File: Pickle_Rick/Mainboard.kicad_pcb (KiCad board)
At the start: 4 copper layers, 152 parts, among them J1 USB_C_Receptacle, J10 Conn_01x02_Male, J11 Conn_01x02_Male, J12 Conn_01x02_Male, J2 8P8C_LED, J3 Micro_SD_Card_Det, J4 Conn_Coaxial, J5 Conn_Coaxial, J6 Screw_Terminal_01x02, J7 Screw_Terminal_01x02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

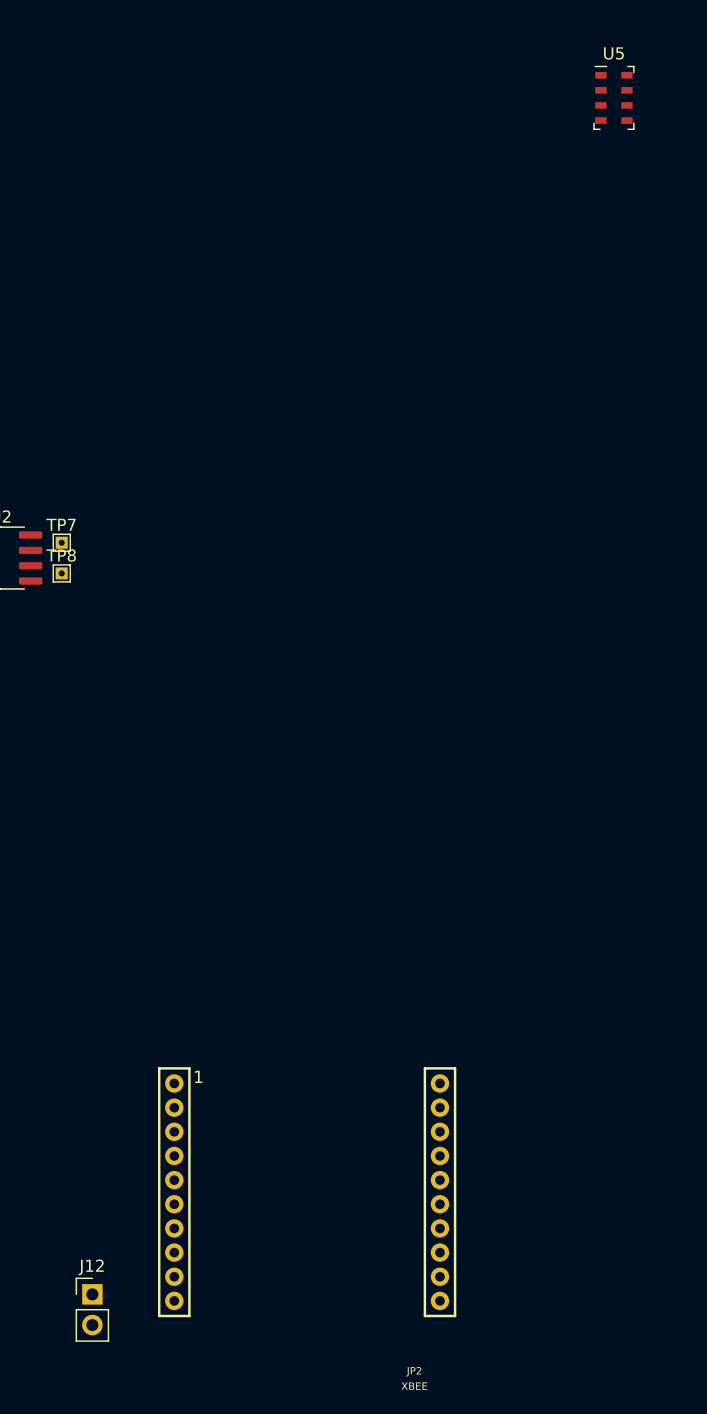
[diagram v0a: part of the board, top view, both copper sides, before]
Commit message: changed usb 2.0 to 3.0; started pcb design; changed flash symbol
need to change flash footprint still
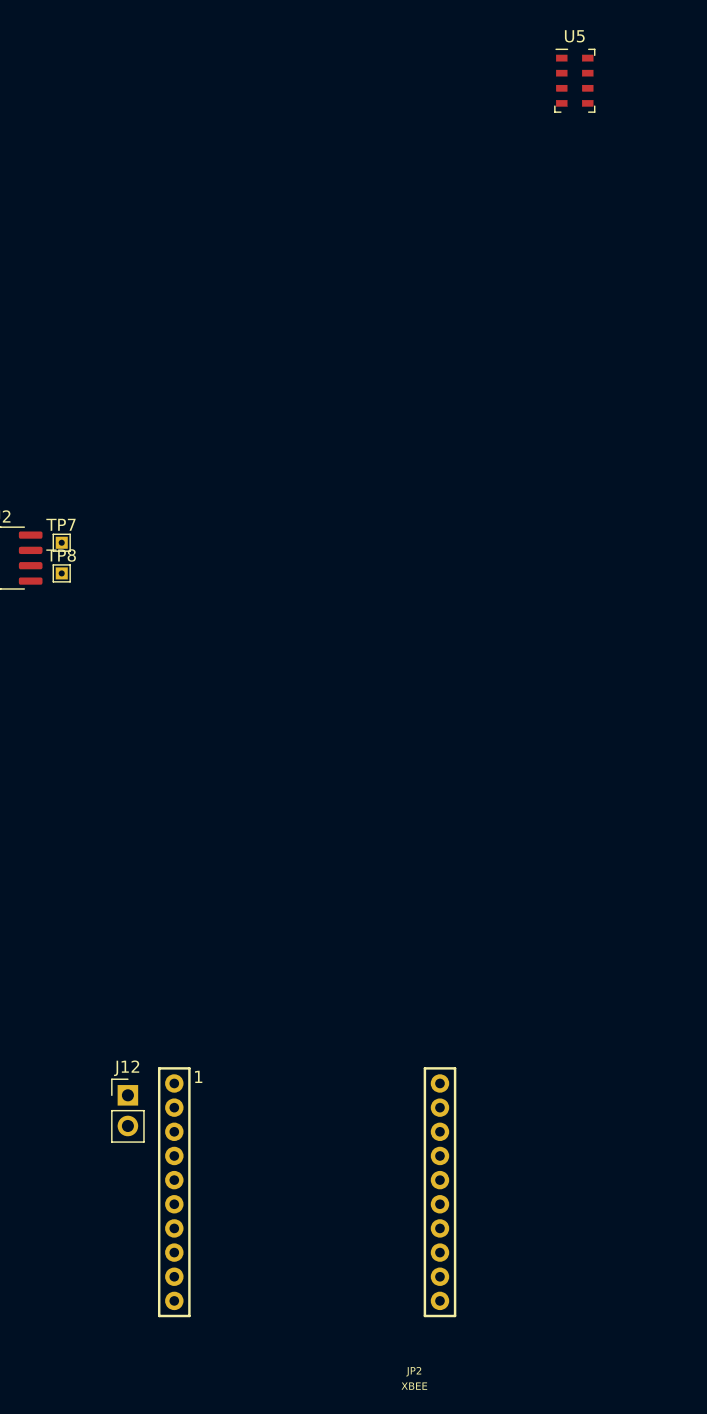
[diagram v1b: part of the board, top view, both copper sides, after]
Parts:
- moved J12 16.7 mm to (229.0, -113.0)
- moved U5 3.54 mm to (266.0, -197.0)
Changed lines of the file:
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@@
   )
   (module Package_LGA:LGA-8_3x5mm_P1.25mm (layer F.Cu)
-    (at 269.24 -195.58)
+    (at 266 -197)
     (descr LGA-8)
     (tags "lga land grid array")
@@
   )
   (module Connector_PinHeader_2.54mm:PinHeader_1x02_P2.54mm_Vertical (layer F.Cu)
-    (at 226.06 -96.52)
+    (at 229 -113)
     (descr "Through hole straight pin header, 1x02, 2.54mm pitch, single row")
     (tags "Through hole pin header THT 1x02 2.54mm single row")

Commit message: did some pcb thing
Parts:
- removed H3, H4: MountingHole_Pad, MountingHole:MountingHole_3.2mm_M3_DIN965_Pad
- removed JP2: XBEE, iclr:XBEE
- BZ1: moved to B.Cu
- D13: value USB_LED -> down_led
- D17: value USB_LED -> up_led
- H1, H2: footprint MountingHole:MountingHole_3.2mm_M3_DIN965_Pad -> MountingHole:MountingHole_2.2mm_M2_Pad
- moved R2 406.9 mm to (24.4, 85.8), turned to 270 degrees
- moved R26 403.7 mm to (40.7, 100.0), turned to 180 degrees
- moved TP23 403.2 mm to (34.6, 96.7)
- moved R39 403.0 mm to (37.5, 97.0), turned to 180 degrees
- moved R40 402.4 mm to (37.6, 92.3), turned to 180 degrees
- moved R1 401.9 mm to (28.8, 85.6), turned to 90 degrees
- moved C2 401.5 mm to (37.6, 80.1)
- moved R37 401.1 mm to (38.2, 99.3), turned to 270 degrees
- moved TP19 398.0 mm to (36.4, 98.8)
- moved TP2 396.1 mm to (35.9, 90.4)
- moved TP22 395.9 mm to (43.2, 100.2)
- moved R8 395.3 mm to (61.0, 98.9), turned to 90 degrees
- moved TP20 394.6 mm to (38.0, 90.4)
- moved H1 393.7 mm to (24.9, 106.7)
- moved TP9 388.8 mm to (59.8, 91.5)
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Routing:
- net /MOSI: track 0.00 -> 16.7 mm
- net /RADIO_TX: track 0.00 -> 15.3 mm
- net /MISO: track 0.00 -> 14.8 mm, vias 0 -> 1
- net /LORA_RESET: track 0.00 -> 13.7 mm, vias 0 -> 2
- net /RADIO_RX: track 0.00 -> 10.8 mm
- net /LORA_CS: track 0.00 -> 10.3 mm
- net /Cont2: track 0.00 -> 5.79 mm, vias 0 -> 1
- net /BOOT: track 0.00 -> 5.72 mm, vias 0 -> 1
- net /Cont1: track 0.00 -> 5.64 mm, vias 0 -> 1
- net /SCL: track 0.00 -> 5.41 mm
- net /SDA: track 0.00 -> 4.54 mm
- net /RXD: track 0.00 -> 4.06 mm, vias 0 -> 1
- net /TXD: track 0.00 -> 4.00 mm, vias 0 -> 1
- net +3V3: track 0.00 -> 3.92 mm
- net /SCLK: track 0.00 -> 2.77 mm
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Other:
- board outline added: 100 x 30 mm

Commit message: added critical silkscreen + circuitry around esp mostly done
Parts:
- added G***: LOGO, iclr:pccRicc650dpi, F.Cu at (102.8, 139.4)
- added G***: LOGO, iclr:iclr_logo, F.Cu at (113.0, 134.3)
- moved U10 376.8 mm to (77.2, 31.0)
- moved TP4 358.5 mm to (29.2, 84.3)
- moved TP5 358.5 mm to (25.2, 84.3)
- moved TP6 355.4 mm to (27.3, 86.6)
- moved R4 350.8 mm to (34.0, 88.1)
- moved D1 345.3 mm to (32.7, 82.0), turned to 180 degrees
- moved R3 344.5 mm to (39.0, 86.0)
- moved R6 339.6 mm to (42.1, 86.0), turned to 180 degrees
- moved TP3 338.5 mm to (48.8, 85.5)
- moved D9 325.5 mm to (51.1, 86.3)
- moved R25 322.3 mm to (113.7, 86.5), turned to 180 degrees
- moved C4 320.3 mm to (113.7, 84.9), turned to 180 degrees
- moved J4 319.6 mm to (114.4, 82.0), turned to 90 degrees
- moved L1 315.9 mm to (116.1, 85.7), turned to 270 degrees
- moved U6 308.7 mm to (116.7, 93.4), turned to 90 degrees
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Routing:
- net +3V3: track 3.92 -> 36.0 mm, vias 0 -> 4
- net GND: track 0.00 -> 23.6 mm
- net /EN: track 0.00 -> 12.4 mm
- net /MAG_CS: track 0.00 -> 10.7 mm
- net /LORA_RESET: track 13.7 -> 3.53 mm
- net Net-(C3-Pad1): track 1.44 -> 9.90 mm
- net /MISO: track 14.8 -> 6.63 mm
- net /DTR: track 0.00 -> 6.74 mm
- net /CAN_TX: track 0.00 -> 6.70 mm
- net Net-(R16-Pad2): track 0.00 -> 6.53 mm
- net /IMU_CS: track 0.00 -> 5.26 mm
- net /SD_CS: track 0.00 -> 5.18 mm
- net Net-(D15-Pad1): track 0.00 -> 5.02 mm
- net /FLASH_CS: track 0.00 -> 4.58 mm
- net /BARO_CS: track 0.00 -> 4.36 mm
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- added copper zone on In1.Cu, net +3V3
- added copper zone on B.Cu, net GND
- added copper zone on In2.Cu, net GND
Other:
- board text added: "Apes togheter strong"
- board text added: "Based on:"
- board text added: "Designed by:"
- board text added: "Luis Marques Joao Matias"
- board text added: "MUST PLACE THESE 3 ON TOP"
- board text added: "RiCaRdO"

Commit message: not getting farther...
need to double check the buzzer, DS suggests 2 resistors
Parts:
- removed G***: LOGO, iclr:pccRicc650dpi
- removed G***: LOGO, iclr:iclr_logo
- added R43: 1k, Resistor_SMD:R_0603_1608Metric, F.Cu at (42.3, 118.3)
- moved J1 449.8 mm to (28.2, 84.8), turned to 270 degrees
- moved D13 445.4 mm to (31.3, 91.9)
- moved D17 445.4 mm to (31.3, 93.9)
- moved R42 444.9 mm to (35.9, 94.4), turned to 90 degrees
- moved R41 443.3 mm to (36.9, 85.5)
- moved C5 416.5 mm to (55.9, 102.8), turned to 90 degrees
- moved C6 415.5 mm to (54.4, 102.8), turned to 90 degrees
- moved C8 403.2 mm to (102.0, 175.3), turned to 180 degrees
- moved C7 401.4 mm to (102.0, 181.4), turned to 180 degrees
- moved C9 400.2 mm to (102.0, 176.8), turned to 180 degrees
- moved J11 398.5 mm to (-14.3, 130.9)
- moved U12 398.4 mm to (-10.4, 131.4)
- moved C22 397.1 mm to (19.7, 130.6), turned to 180 degrees
- moved C17 396.7 mm to (22.7, 130.6), turned to 180 degrees
- moved C19 395.5 mm to (19.6, 121.4), turned to 180 degrees
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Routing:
- net GND: track 23.6 -> 59.8 mm
- net +3V3: track 36.0 -> 60.3 mm, vias 4 -> 5
- net Net-(J5-Pad1): track 0.00 -> 17.6 mm, vias 0 -> 2
- net /SDA: track 4.54 -> 16.0 mm, vias 0 -> 2
- net Net-(JP5-Pad2): track 0.00 -> 10.4 mm
- net /SCL: track 5.41 -> 15.8 mm, vias 0 -> 2
- net Net-(R25-Pad2): track 0.00 -> 8.64 mm
- net Net-(J4-Pad1): track 0.00 -> 8.29 mm
- net /GPS/RXD: track 0.00 -> 8.24 mm
- net /RADIO_RX: track 11.0 -> 2.81 mm
- net Net-(C6-Pad1): track 0.00 -> 7.27 mm
- net /FLASH_CS: track 4.58 -> 10.4 mm, vias 0 -> 1
- net /BOOT: track 5.45 -> 11.2 mm, vias 1 -> 2
- net Net-(R23-Pad2): track 0.00 -> 4.85 mm
- net Net-(D15-Pad1): track 5.02 -> 0.17 mm
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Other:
- board text removed: "MUST PLACE THESE 3 ON TOP"

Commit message: it almost fits (☉_☉) ...
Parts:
- added G***: LOGO, iclr:pccRicc650dpi, F.Cu at (33.4, 159.3)
- added G***: LOGO, iclr:iclr_logo, F.Cu at (47.1, 151.0)
- J11, U12: moved to B.Cu
- moved J3 122.0 mm to (150.1, 101.8)
- moved TP16 114.7 mm to (34.4, 98.4), turned to 180 degrees
- moved C31 114.3 mm to (32.6, 99.4)
- moved C7 113.1 mm to (30.2, 94.0), turned to 0 degrees
- moved C10 111.8 mm to (34.8, 100.2), turned to 180 degrees
- moved U8 110.8 mm to (30.7, 102.8), turned to 180 degrees
- moved C11 110.7 mm to (30.2, 95.5), turned to 0 degrees
- moved C30 108.4 mm to (30.2, 97.1), turned to 0 degrees
- moved TP17 106.7 mm to (103.9, 74.3), turned to 180 degrees
- moved C9 106.1 mm to (30.2, 98.6), turned to 0 degrees
- moved L2 105.7 mm to (34.5, 102.9), turned to 270 degrees
- moved C8 103.9 mm to (30.3, 100.1), turned to 0 degrees
- moved R14 85.8 mm to (32.5, 96.4), turned to 270 degrees
- moved D6 85.5 mm to (33.5, 94.0)
- moved D12 65.9 mm to (49.1, 99.5), turned to 90 degrees
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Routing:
- net Net-(C6-Pad1): track 7.27 -> 106.5 mm, vias 0 -> 2
- net /MAG_CS: track 9.08 -> 87.3 mm, vias 0 -> 1
- net Net-(C5-Pad1): track 3.95 -> 77.4 mm, vias 0 -> 2
- net /IMU_CS: track 10.00 -> 82.0 mm, vias 0 -> 1
- net GND: track 59.8 -> 126.3 mm
- net /SCLK: track 7.36 -> 59.8 mm
- net /LORA_INT: track 3.61 -> 45.3 mm
- net /MISO: track 9.96 -> 46.3 mm
- net +3V3: track 60.3 -> 95.5 mm, vias 5 -> 8
- net Net-(C1-Pad1): track 2.29 -> 37.5 mm
- net /BOOT: track 11.2 -> 45.3 mm
- net /TXD: track 4.18 -> 37.8 mm
- net /RXD: track 4.44 -> 34.8 mm
- net /usb-c/usb_VBUS: track 3.90 -> 31.3 mm
- net /LORA_RESET: track 4.75 -> 26.0 mm
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- removed copper zone on B.Cu, net GND
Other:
- board size 100 x 30 mm -> 100.1 x 30.1 mm
- board text added: "to the moon"

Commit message: todo: change everything ᕙ(⇀‸↼‶)ᕗ
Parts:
- removed BZ1: Buzzer, Buzzer_Beeper:Buzzer_TDK_PS1240P02BT_D12.2mm_H6.5mm
- removed G***: LOGO, iclr:pccRicc650dpi
- removed G***: LOGO, iclr:iclr_logo
- added J13: Conn_01x02, Connector_JST:JST_XH_B2B-XH-A_1x02_P2.50mm_Vertical, F.Cu at (91.1, 116.5)
- J5: footprint Connector_Coaxial:SMA_Molex_73251-1153_EdgeMount_Horizontal -> Connector_Coaxial:U.FL_Hirose_U.FL-R-SMT-1_Vertical
- J6, J7, J8: footprint iclr:PHOENIX_1757242 -> TerminalBlock_Phoenix:TerminalBlock_Phoenix_PT-1,5-2-5.0-H_1x02_P5.00mm_Horizontal
- moved J5 16.5 mm to (105.3, 68.5)
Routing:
- net /MOSI: track 18.3 -> 5.23 mm
- net /RADIO_TX: track 14.6 -> 4.10 mm
- net GND: track 126.3 -> 116.6 mm
- net /LORA_CS: track 10.2 -> 6.08 mm
- net Net-(J5-Pad1): track 18.3 -> 15.1 mm, vias 2 -> 1

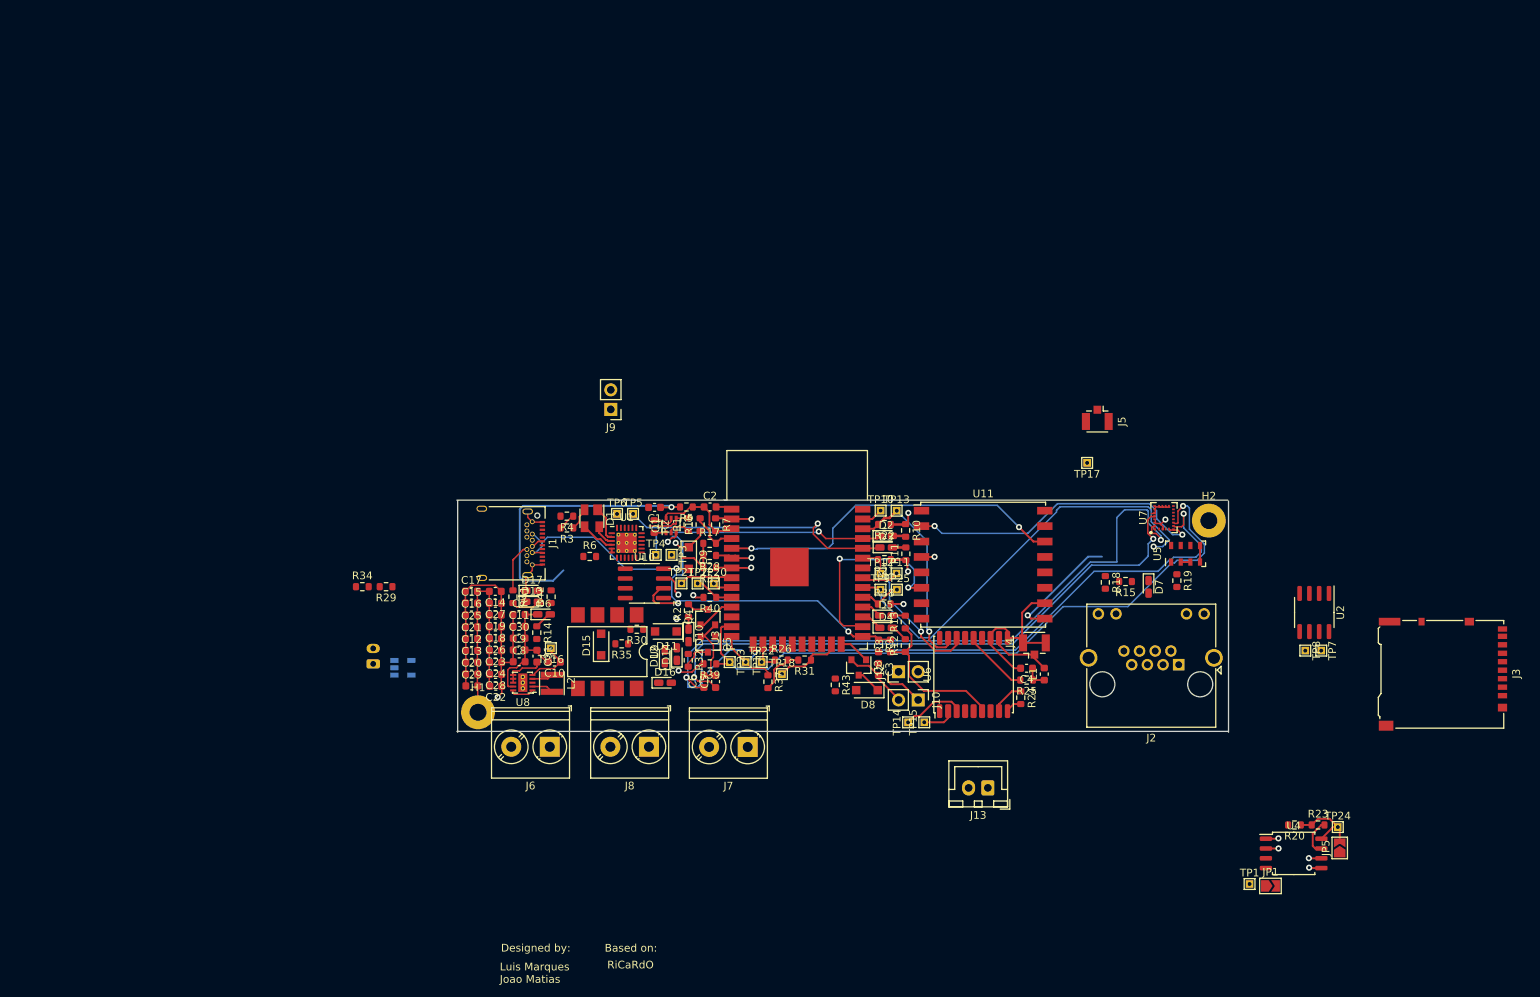
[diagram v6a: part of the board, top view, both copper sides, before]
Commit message: fixed rbg port
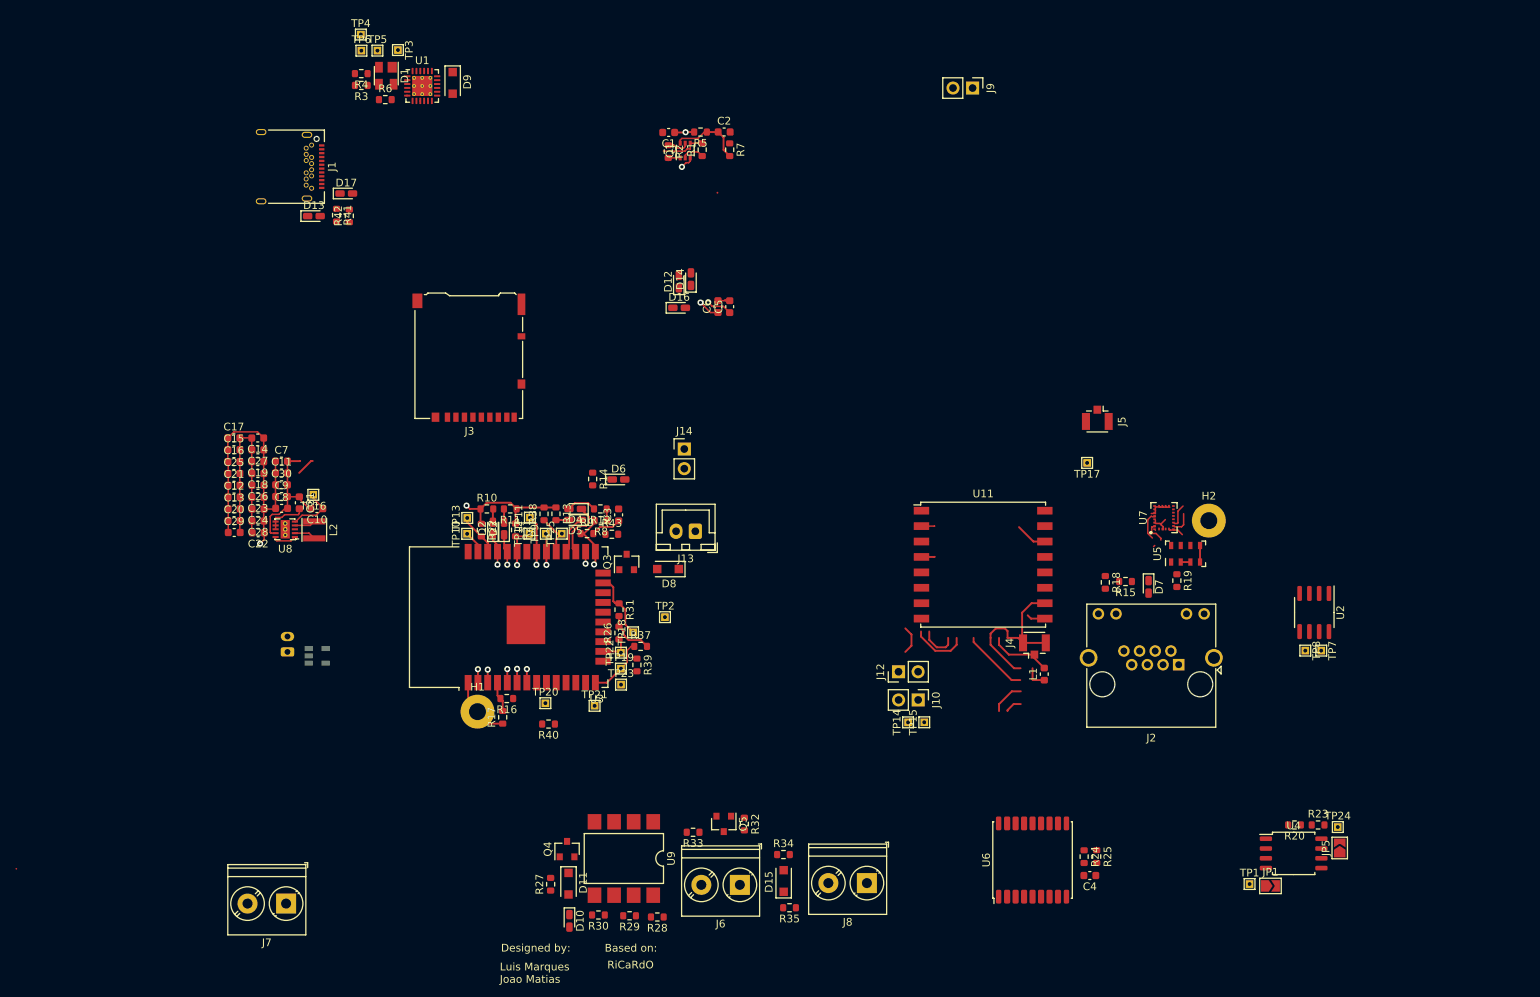
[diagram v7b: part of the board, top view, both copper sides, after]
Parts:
- removed U10: PCA9536D, Package_SO:SOIC-8_3.9x4.9mm_P1.27mm
- added J14: Conn_01x02_Male, Connector_PinHeader_2.54mm:PinHeader_1x02_P2.54mm_Vertical, F.Cu at (51.7, 72.5)
- moved J3 132.9 mm to (23.7, 60.7), turned to 180 degrees
- moved TP4 77.6 mm to (9.72, 18.8)
- moved TP3 74.5 mm to (14.5, 20.8)
- moved D9 68.8 mm to (21.6, 25.0)
- moved TP5 68.6 mm to (11.9, 20.9)
- moved TP6 68.6 mm to (9.79, 20.9)
- moved R6 64.9 mm to (12.9, 27.2)
- moved U1 64.9 mm to (17.7, 25.4)
- moved R34 64.7 mm to (64.5, 125.2)
- moved D1 63.3 mm to (13.0, 24.1)
- moved R3 63.3 mm to (9.78, 25.4)
- moved R4 63.3 mm to (9.78, 23.8)
- moved J7 63.2 mm to (0.02, 131.5)
- moved J9 62.8 mm to (89.1, 25.7), turned to 270 degrees
- moved D13 57.5 mm to (3.63, 42.3)
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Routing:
- net Net-(C6-Pad1): track 106.5 -> 5.73 mm, vias 2 -> 1
- net /MAG_CS: track 87.3 -> 3.30 mm, vias 1 -> 0
- net /IMU_CS: track 82.0 -> 11.2 mm, vias 1 -> 0
- net Net-(C5-Pad1): track 77.4 -> 7.05 mm, vias 2 -> 1
- net /SCLK: track 59.8 -> 6.37 mm, vias 3 -> 1
- net /LORA_INT: track 45.3 -> 5.08 mm, vias 2 -> 1
- net /MISO: track 46.3 -> 10.5 mm, vias 3 -> 1
- net Net-(C1-Pad1): track 37.5 -> 2.29 mm
- net GND: track 116.6 -> 81.9 mm
- net /BOOT: track 45.3 -> 11.5 mm
- net /TXD: track 37.8 -> 6.10 mm
- net /usb-c/usb_VBUS: track 31.3 -> 2.13 mm, vias 1 -> 0
- net /RXD: track 34.8 -> 6.19 mm
- net /LORA_RESET: track 26.0 -> 1.56 mm, vias 2 -> 1
- net /SCL: track 33.5 -> 10.4 mm, vias 2 -> 0
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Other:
- board outline removed

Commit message: quite the pickle
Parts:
- added G***: LOGO, iclr:pccRicc650dpi, F.Cu at (246.4, 43.1)
- added G***: LOGO, iclr:iclr_logo, F.Cu at (231.2, 39.0)
- J11, U12: moved to F.Cu
- moved C8 141.9 mm to (140.8, 68.4)
- moved C9 141.7 mm to (140.9, 70.0)
- moved C7 141.5 mm to (140.8, 66.8)
- moved J1 96.2 mm to (82.3, 85.1), turned to 180 degrees
- moved D1 92.7 mm to (93.6, 69.9)
- moved D9 92.7 mm to (102.2, 70.9)
- moved R3 92.7 mm to (90.4, 71.2)
- moved R4 92.7 mm to (90.4, 69.7)
- moved R6 92.7 mm to (93.5, 73.0)
- moved TP3 92.7 mm to (95.1, 66.6)
- moved TP4 92.7 mm to (90.3, 64.6)
- moved TP5 92.7 mm to (92.5, 66.7)
- moved TP6 92.7 mm to (90.4, 66.7)
- moved U1 92.7 mm to (98.3, 71.3)
- moved C6 89.0 mm to (143.4, 70.8)
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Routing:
- net /nukes/External_Supply: track 0.00 -> 75.2 mm, vias 0 -> 1
- net /RADIO_RX: track 7.56 -> 38.9 mm, vias 0 -> 1
- net Net-(D11-Pad2): track 0.00 -> 30.3 mm, vias 0 -> 1
- net Net-(D15-Pad2): track 0.00 -> 30.2 mm
- net /SCL: track 10.4 -> 39.9 mm
- net /RADIO_TX: track 6.41 -> 35.5 mm, vias 0 -> 1
- net Net-(C3-Pad1): track 3.96 -> 32.7 mm, vias 0 -> 1
- net /Cont1: track 0.98 -> 22.4 mm, vias 1 -> 2
- net GND: track 81.9 -> 101.9 mm
- net /Cont2: track 1.08 -> 18.7 mm, vias 1 -> 2
- net Net-(J11-Pad1): track 0.00 -> 17.5 mm, vias 0 -> 1
- net /SDA: track 13.6 -> 30.7 mm
- net Net-(R34-Pad1): track 0.00 -> 15.7 mm
- net /Nuke2: track 1.50 -> 17.1 mm, vias 0 -> 2
- net /MAG_CS: track 3.30 -> 14.3 mm
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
